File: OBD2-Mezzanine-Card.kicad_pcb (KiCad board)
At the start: 2 copper layers, 87.5 x 54 mm, 65 parts, among them IC1 ELM327, J1 OBD2-DB9_Male, P1 CONN_02X20, P2 CONN_02X20, Q1 2N3904, Q2 2N3906, Q3 2N3906, Q4 2N3904, Q5 2N3904, Q6 2N3904, Q7 2N3904, U1 MCP2561-E/P, U2 LM317L_TO92, Y1 4.0MHz

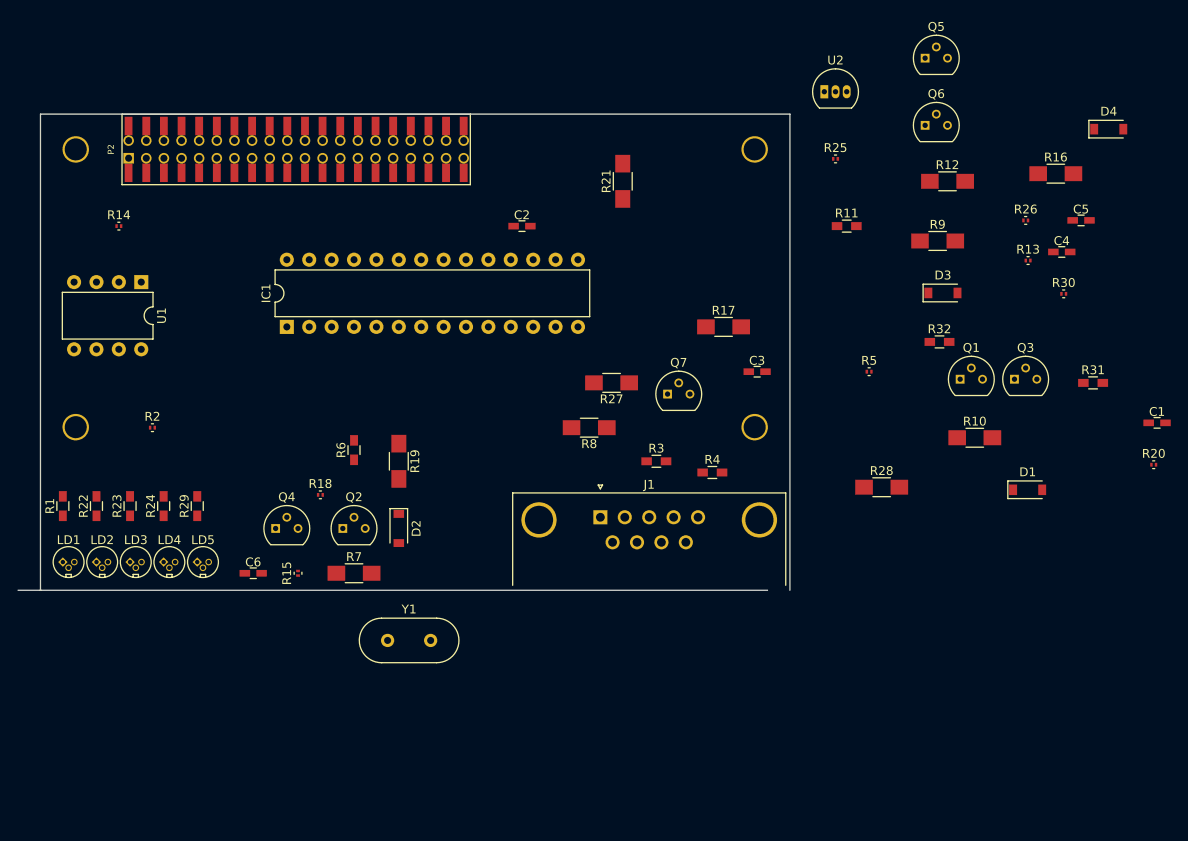
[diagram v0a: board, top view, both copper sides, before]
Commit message: kicad_pcb: Start to connect tracks
Signed-off-by: Alistair Francis <alistair@alistair23.me>
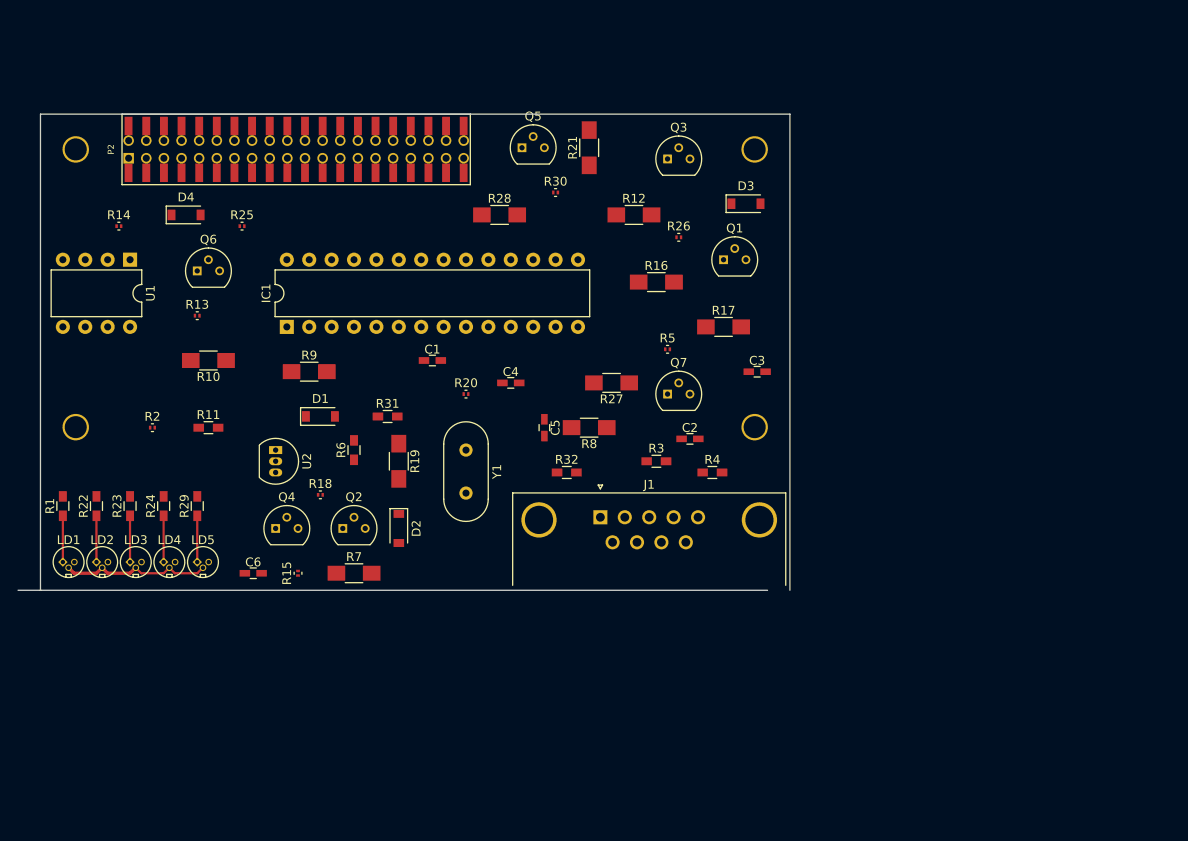
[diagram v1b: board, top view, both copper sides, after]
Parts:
- moved D4 105.1 mm to (116.5, 111.4)
- moved R13 94.4 mm to (117.8, 122.9)
- moved R10 87.4 mm to (119.0, 127.9), turned to 180 degrees
- moved Q6 84.2 mm to (117.8, 117.8)
- moved C1 82.5 mm to (144.4, 127.9)
- moved D1 80.6 mm to (131.8, 134.3)
- moved R31 80.1 mm to (139.4, 134.3)
- moved R20 78.4 mm to (148.3, 131.8)
- moved R11 75.9 mm to (119.0, 135.6)
- moved U2 74.3 mm to (126.7, 138.1), turned to 270 degrees
- moved R9 72.8 mm to (130.5, 129.2)
- moved R25 67.7 mm to (122.9, 112.7)
- moved C5 65.3 mm to (157.2, 135.6), turned to 270 degrees
- moved C4 64.2 mm to (153.3, 130.5)
- moved R30 58.8 mm to (158.4, 108.9)
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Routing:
- net +5V: track 0.00 -> 17.3 mm
- net Net-(LD5-Pad1): track 0.00 -> 5.25 mm
- net Net-(LD4-Pad1): track 0.00 -> 5.25 mm
- net Net-(LD3-Pad1): track 0.00 -> 5.25 mm
- net Net-(LD2-Pad1): track 0.00 -> 5.25 mm
- net Net-(LD1-Pad1): track 0.00 -> 5.25 mm

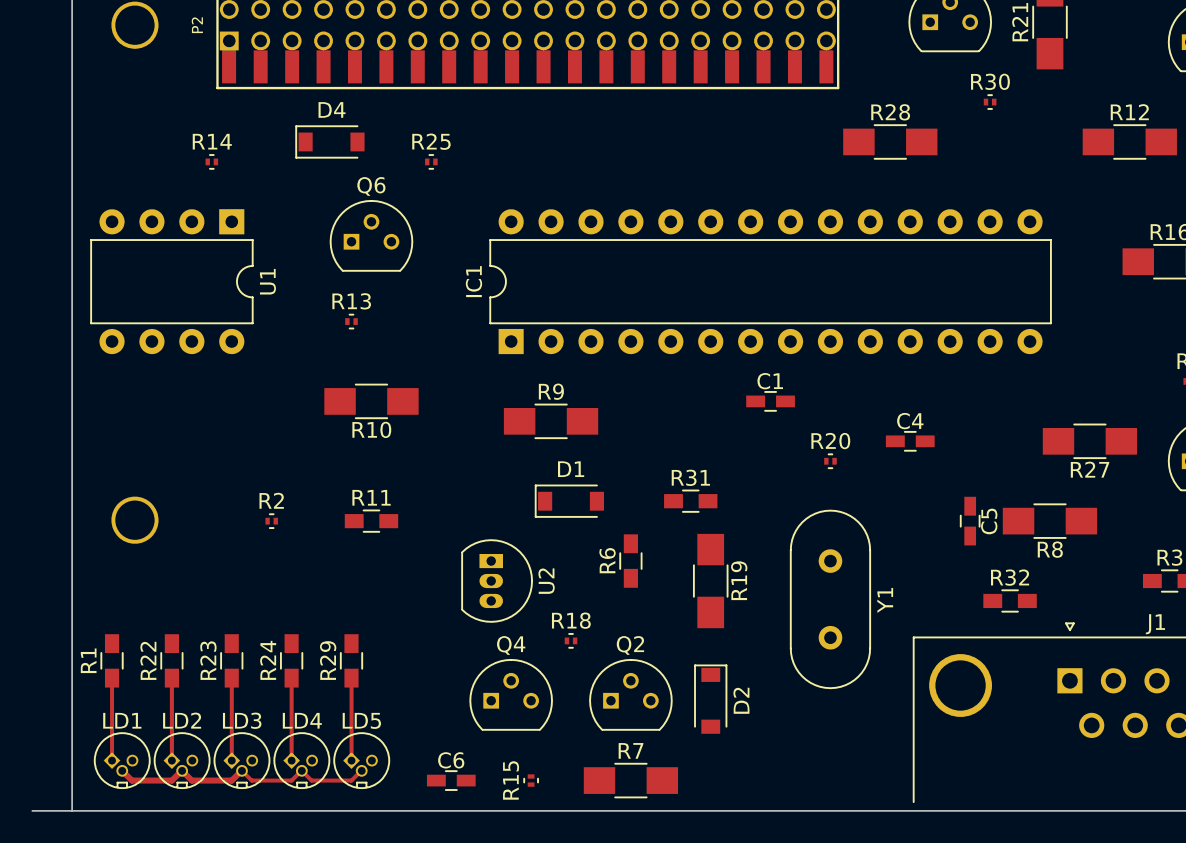
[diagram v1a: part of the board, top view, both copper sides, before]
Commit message: kicad_pcb: Continue to connect tracks
Signed-off-by: Alistair Francis <alistair@alistair23.me>
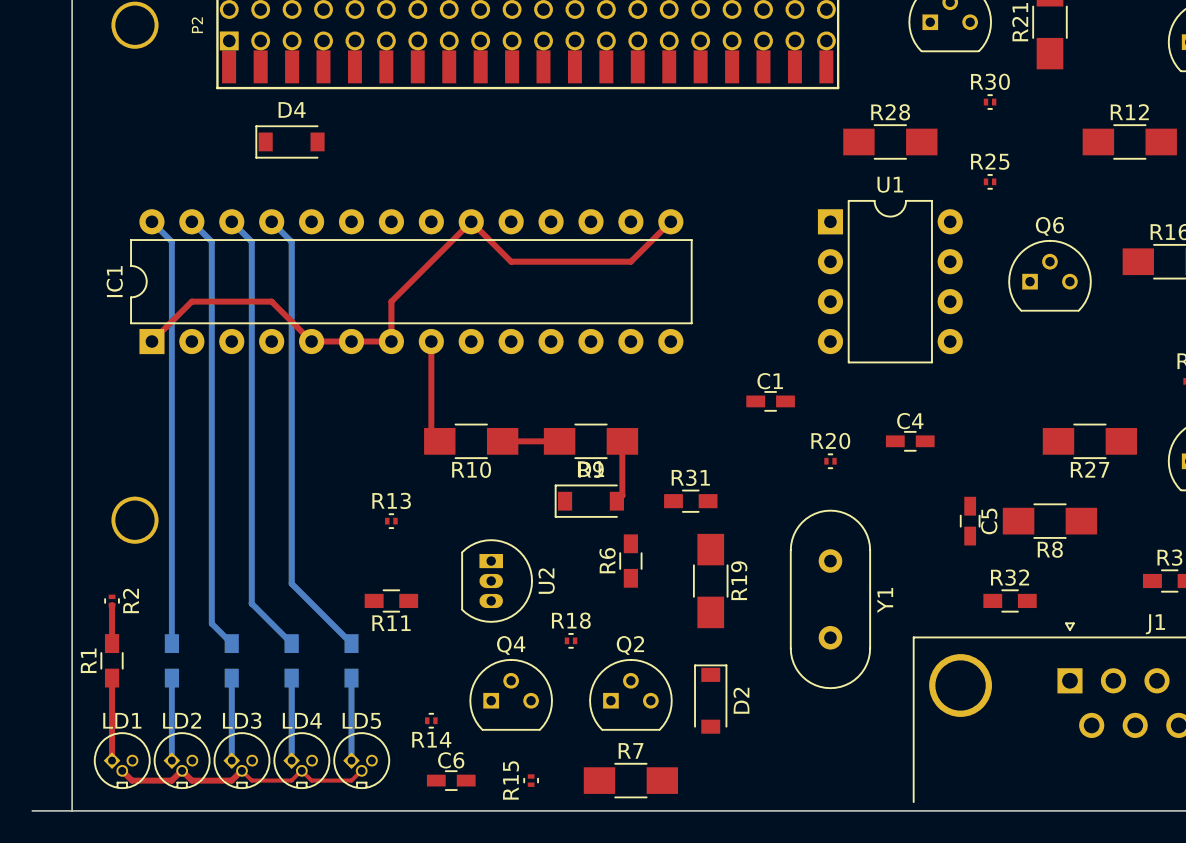
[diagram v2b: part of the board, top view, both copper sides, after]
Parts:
- R22, R23, R24, R29: moved to B.Cu
- moved Q6 43.3 mm to (161.0, 120.3)
- moved R14 38.2 mm to (122.9, 148.3), turned to 180 degrees
- moved U1 38.1 mm to (148.3, 116.5), turned to 0 degrees
- moved R25 35.6 mm to (158.4, 114.0)
- moved IC1 22.9 mm to (105.1, 124.1)
- moved R13 13.0 mm to (120.3, 135.6)
- moved R2 11.4 mm to (102.5, 140.6), turned to 270 degrees
- moved R10 6.84 mm to (125.4, 130.5)
- moved R11 5.24 mm to (120.3, 140.6), turned to 180 degrees
- moved R9 2.84 mm to (133.0, 130.5), turned to 180 degrees
- moved D4 2.54 mm to (114.0, 111.4)
- moved D1 1.27 mm to (133.0, 134.3)
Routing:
- net +5V: track 17.3 -> 59.2 mm
- net Net-(IC1-Pad25): track 0.00 -> 28.9 mm
- net Net-(IC1-Pad26): track 0.00 -> 28.4 mm
- net Net-(IC1-Pad27): track 0.00 -> 27.9 mm
- net Net-(IC1-Pad28): track 0.00 -> 27.4 mm
- net GND: track 0.00 -> 6.57 mm
- net Vbat: track 0.00 -> 3.95 mm
- net Net-(C6-Pad1): track 0.00 -> 3.62 mm
- net PwrCntrl: track 0.00 -> 2.45 mm

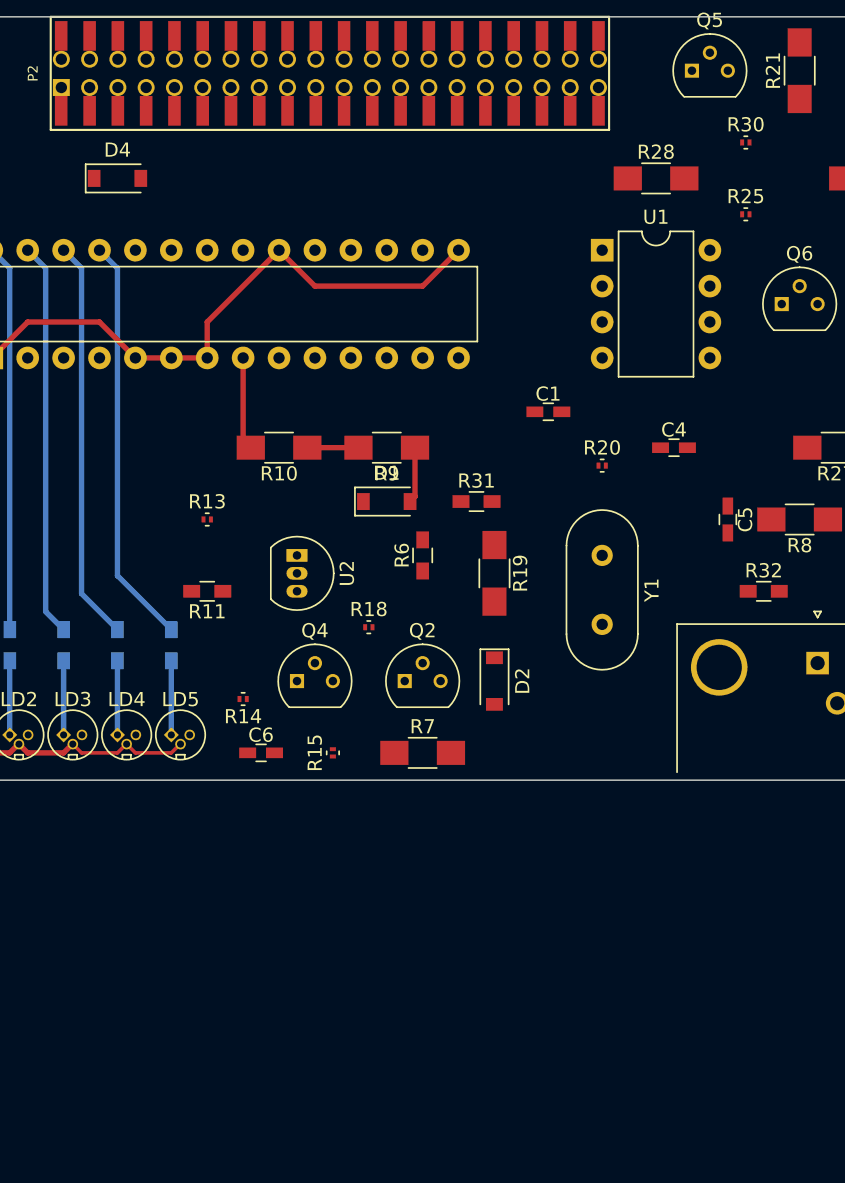
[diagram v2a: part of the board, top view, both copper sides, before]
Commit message: kicad_pcb: Keep connecting
Signed-off-by: Alistair Francis <alistair@alistair23.me>
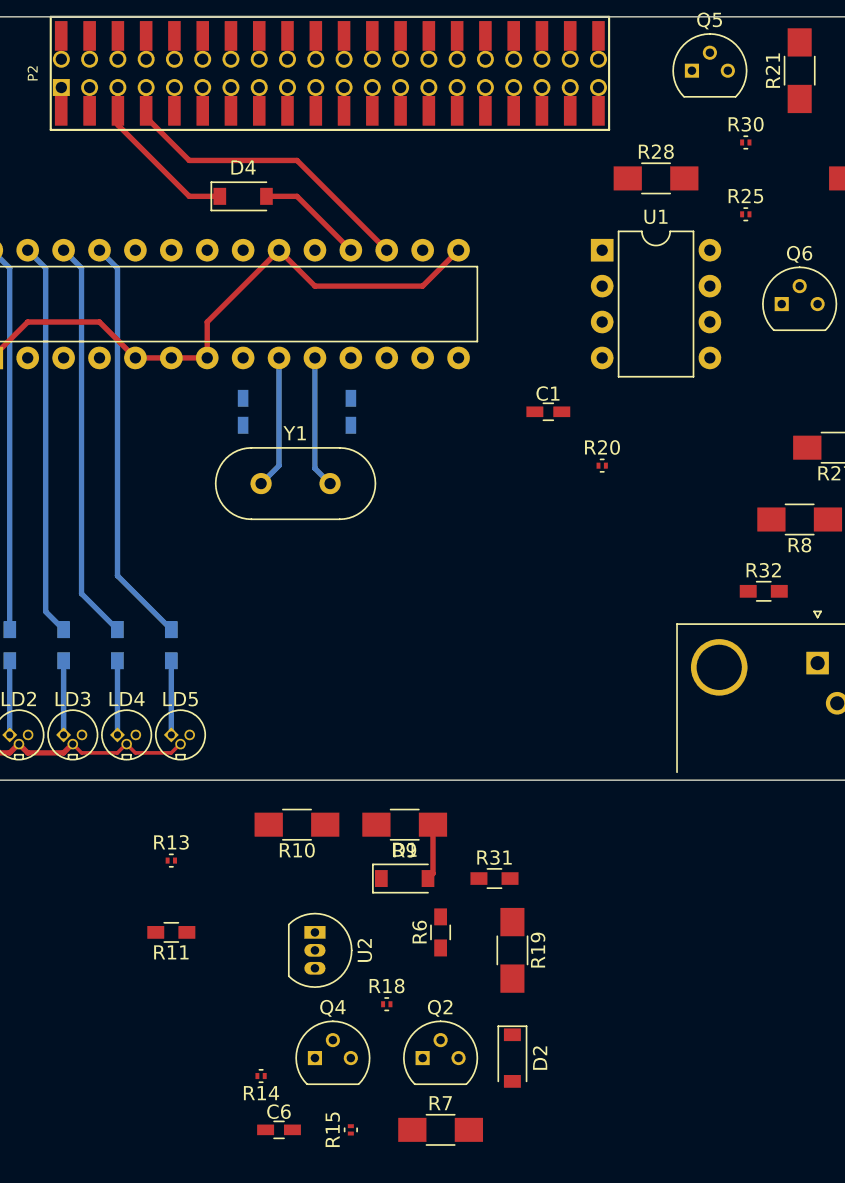
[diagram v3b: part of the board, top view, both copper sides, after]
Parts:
- C4, C5: moved to B.Cu
- moved C4 30.6 mm to (122.9, 127.9), turned to 90 degrees
- moved C5 27.7 mm to (130.5, 127.9), turned to 90 degrees
- moved C6 26.7 mm to (125.4, 178.7)
- moved D1 26.7 mm to (134.3, 161.0)
- moved R10 26.7 mm to (126.7, 157.2)
- moved R14 26.7 mm to (124.1, 174.9)
- moved R15 26.7 mm to (130.5, 178.7)
- moved R31 26.7 mm to (140.6, 161.0)
- moved R6 26.7 mm to (136.8, 164.8)
- moved R7 26.7 mm to (136.8, 178.7)
- moved R9 26.7 mm to (134.3, 157.2)
- moved U2 26.7 mm to (127.9, 164.8)
- moved D2 26.7 mm to (141.9, 173.7)
- moved Q2 26.7 mm to (135.6, 173.7)
- moved Q4 26.7 mm to (127.9, 173.7)
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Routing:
- net UART0_RX: track 0.00 -> 23.0 mm
- net UART0_TX: track 0.00 -> 12.0 mm
- net Net-(C4-Pad1): track 0.00 -> 9.42 mm
- net Net-(C5-Pad1): track 0.00 -> 9.33 mm
- net Net-(D4-Pad2): track 0.00 -> 7.55 mm
- net GND: track 6.57 -> 0.76 mm
- net Net-(C6-Pad1): track 3.62 -> 0.00 mm

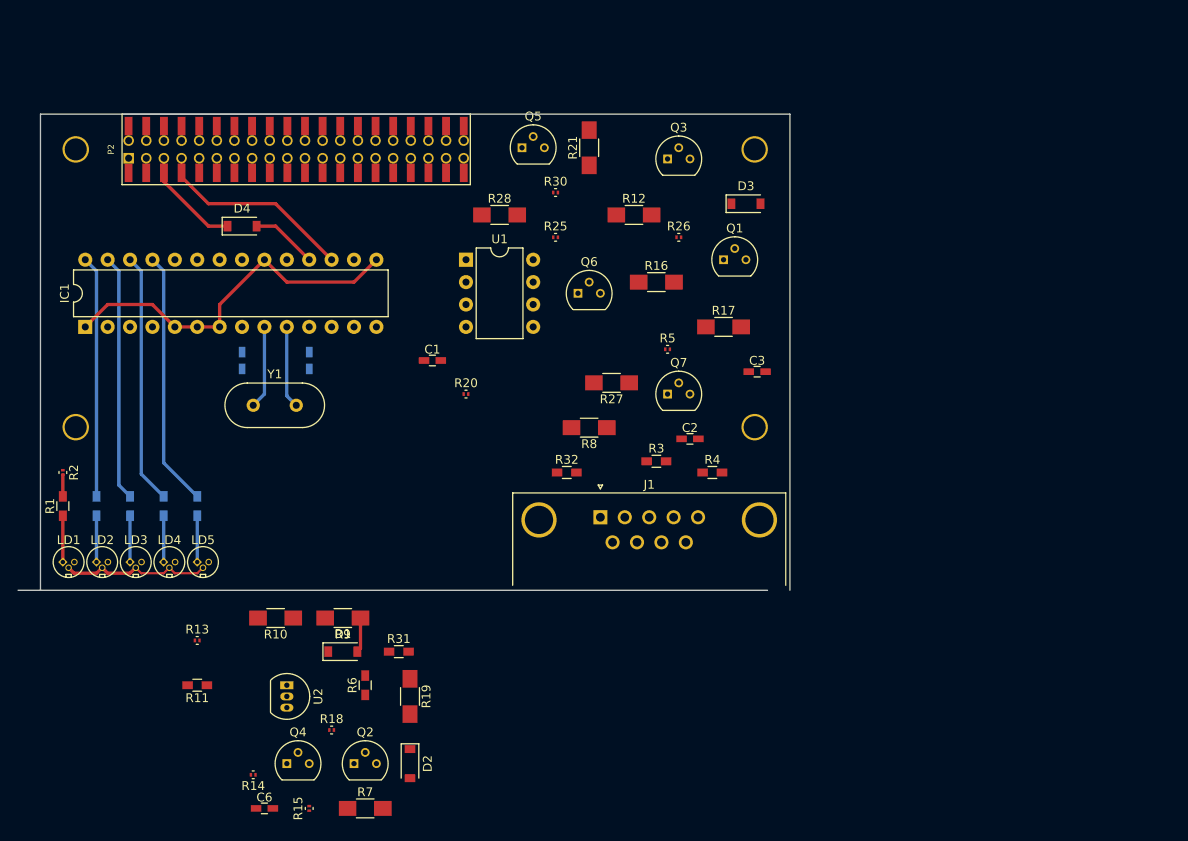
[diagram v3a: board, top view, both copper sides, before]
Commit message: kicad_pcb: Connect a large number of PCB devices
Signed-off-by: Alistair Francis <alistair@alistair23.me>
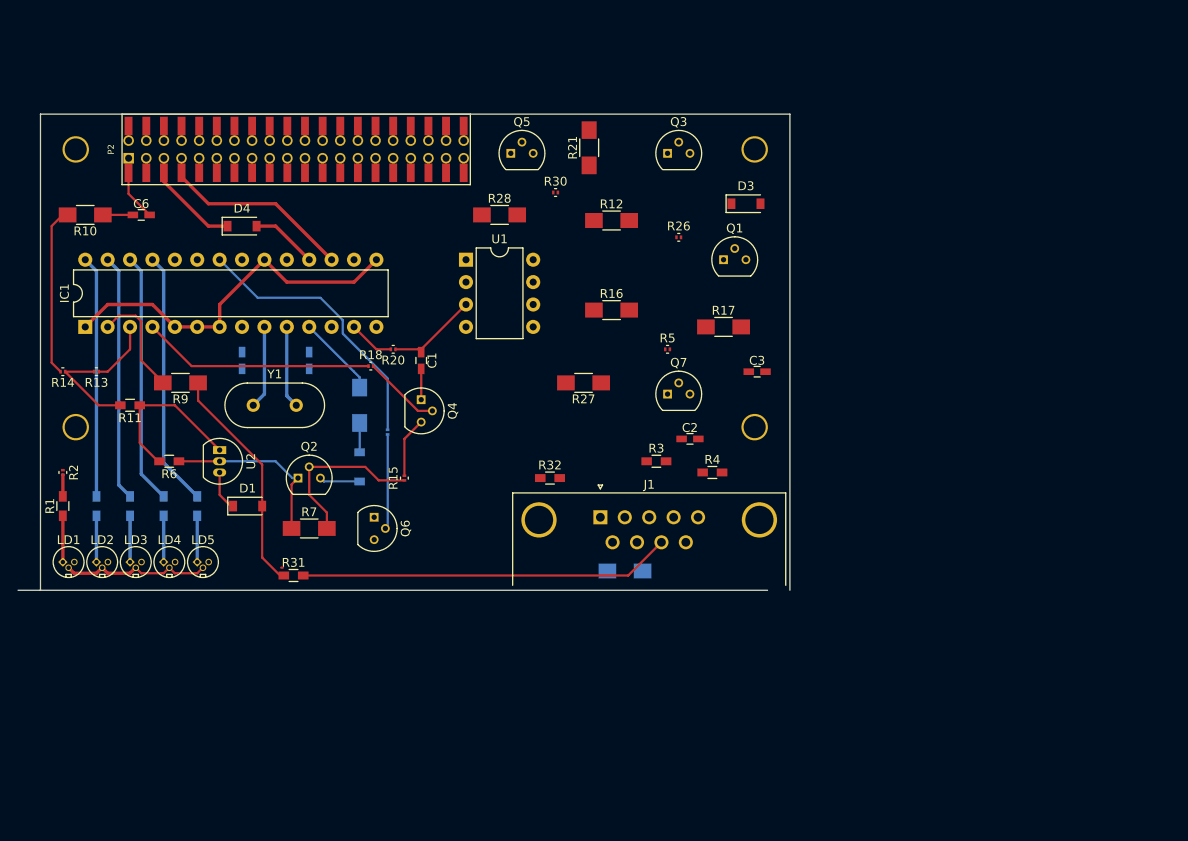
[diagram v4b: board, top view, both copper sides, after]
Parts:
- D2, R19, R25, R8: moved to B.Cu
- moved C6 68.7 mm to (111.4, 111.4)
- moved R10 50.6 mm to (105.1, 111.4)
- moved R14 50.6 mm to (102.5, 129.2)
- moved Q4 44.0 mm to (143.2, 132.4), turned to 270 degrees
- moved R18 41.5 mm to (137.5, 128.6)
- moved R15 39.0 mm to (141.3, 141.3)
- moved Q6 34.3 mm to (137.8, 145.7), turned to 270 degrees
- moved D2 34.1 mm to (136.2, 140.0)
- moved R6 33.8 mm to (114.6, 139.4), turned to 180 degrees
- moved R19 33.5 mm to (136.2, 133.0)
- moved Q2 33.0 mm to (129.2, 141.3)
- moved R11 32.7 mm to (110.2, 133.0)
- moved R13 32.6 mm to (106.3, 129.2), turned to 180 degrees
- moved R9 32.4 mm to (115.9, 130.5)
- moved R7 32.4 mm to (130.5, 147.0)
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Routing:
- net ISO9141-2_L: track 0.00 -> 42.2 mm
- net Net-(IC1-Pad22): track 0.00 -> 31.4 mm
- net GND: track 0.76 -> 28.5 mm
- net Net-(IC1-Pad4): track 0.00 -> 26.3 mm
- net Vbat: track 3.95 -> 26.1 mm
- net Net-(Q2-Pad1): track 0.00 -> 20.3 mm
- net Net-(Q2-Pad2): track 0.00 -> 19.2 mm
- net Net-(R11-Pad1): track 0.00 -> 18.5 mm
- net Net-(C6-Pad1): track 0.00 -> 16.0 mm
- net Net-(R11-Pad2): track 0.00 -> 11.1 mm
- net Net-(Q6-Pad2): track 0.00 -> 10.8 mm
- net +5V: track 59.2 -> 69.7 mm
- net Net-(IC1-Pad11): track 0.00 -> 9.26 mm
- net Net-(Q4-Pad2): track 0.00 -> 8.83 mm
- net Net-(IC1-Pad3): track 0.00 -> 7.14 mm
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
